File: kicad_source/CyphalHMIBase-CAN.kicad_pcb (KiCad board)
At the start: 2 copper layers, 58 x 55 mm, 62 parts, among them CN1 SM04B-SRSS-TB, CN2 DNI, CN3 SM04B-SRSS-TB, CN4 RASPBERRYPI_PICO, CN5 SM04B-GHS-TB, CN6 SM04B-GHS-TB, J1 Conn_01x08, J2 SD_Card_Device, SW1 PTS636 SM43 SMTR LFS, SW2 SW_Push, SW3 RotaryEncoder_Switch_MP, U1 M24C64-RMN6TP, U2 MCP2515T-I/SO, U3 SN65HVD230, Y1 X322516MLB4SI

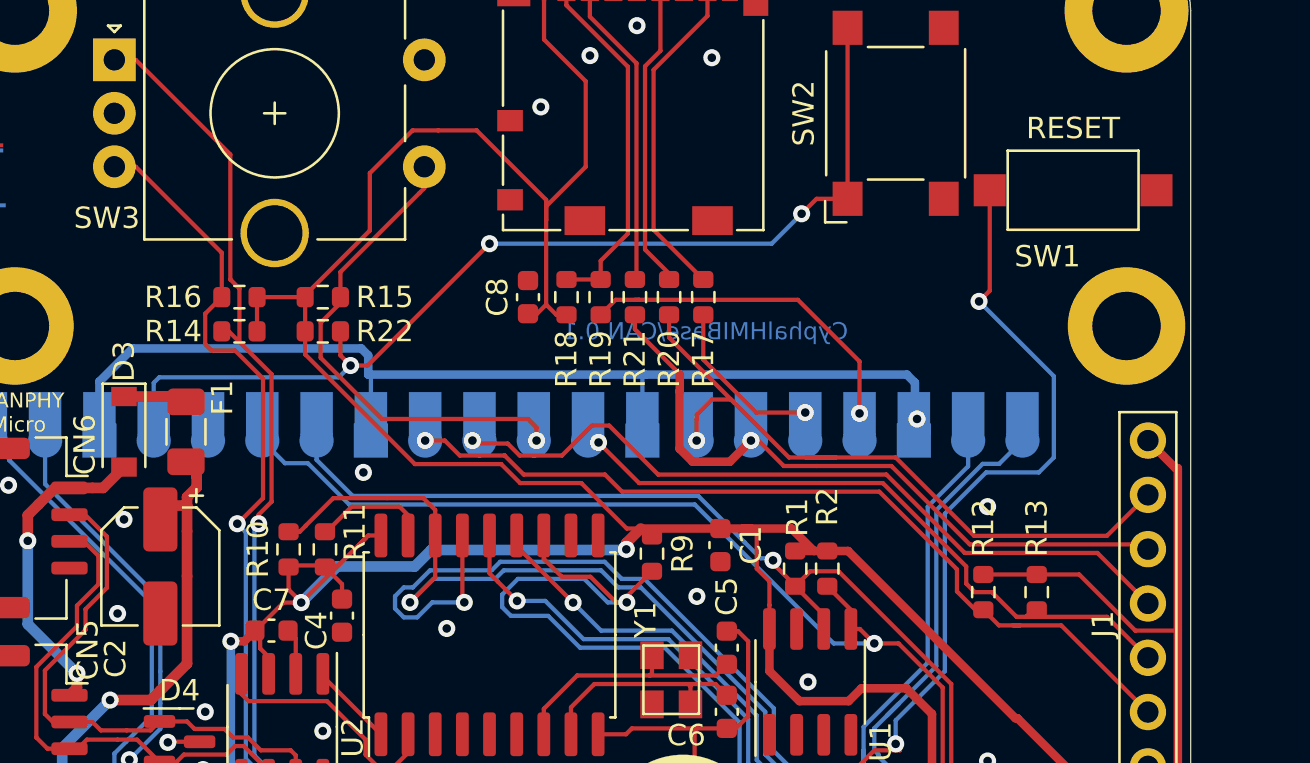
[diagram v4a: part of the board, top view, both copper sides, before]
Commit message: added backlight control
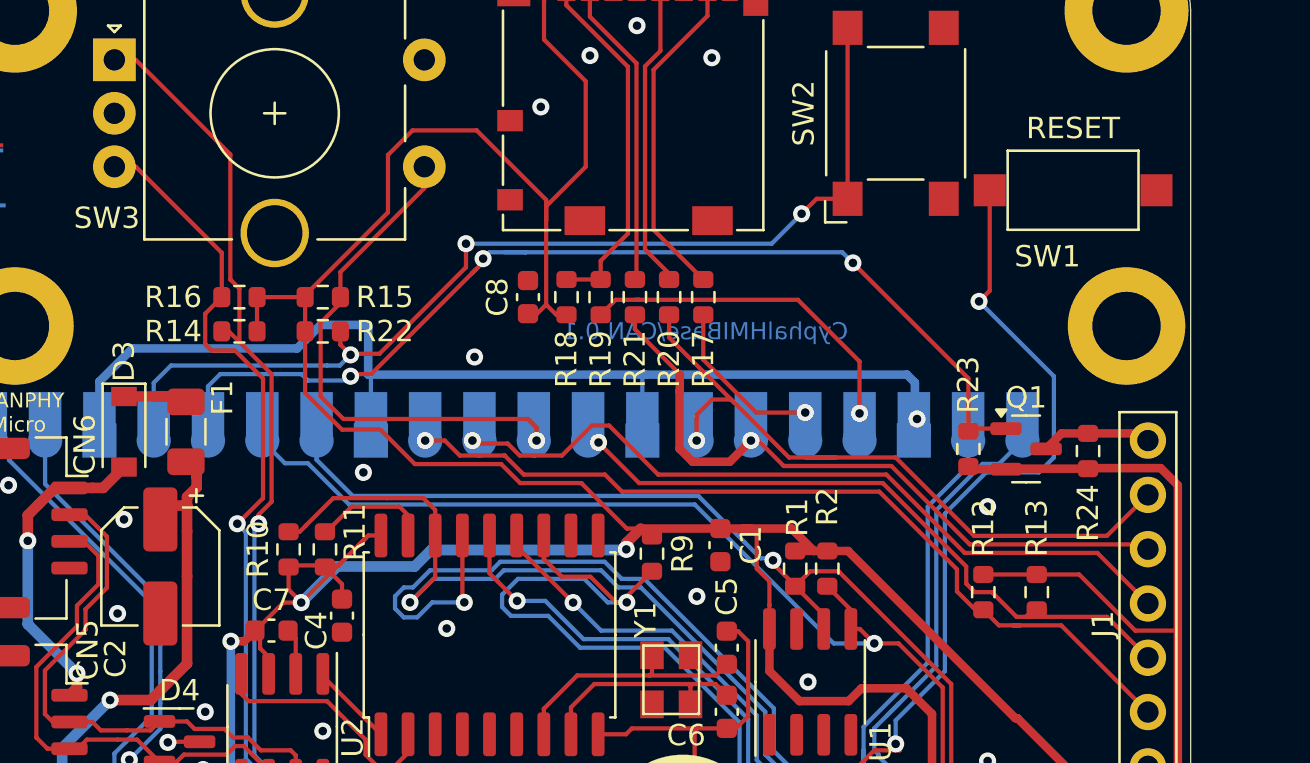
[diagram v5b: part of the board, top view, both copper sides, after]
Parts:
- added Q1: PMOS, Package_TO_SOT_SMD:SOT-23, F.Cu at (114.3, 83.5)
- added R23: 10k, Resistor_SMD:R_0603_1608Metric, F.Cu at (111.6, 83.5)
- added R24: DNI, Resistor_SMD:R_0603_1608Metric, F.Cu at (117.2, 83.6)
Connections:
- CN4 pad 5: unconnected-(CN4-GP3/SPI0_TX/I2C1_SCL-Pad5) -> TFT_BKLT
- J1 pad 8: +3V3 -> /Display/TFT_BKLT_Q
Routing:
- net TFT_BKLT: track 0.00 -> 49.3 mm, vias 0 -> 3
- net +3V3: track 216.7 -> 225.2 mm
- net /Display/TFT_BKLT_Q: track 0.00 -> 5.20 mm
- net GND: track 96.7 -> 98.4 mm, vias 23 -> 24
- net ROT_SW: track 24.3 -> 25.3 mm

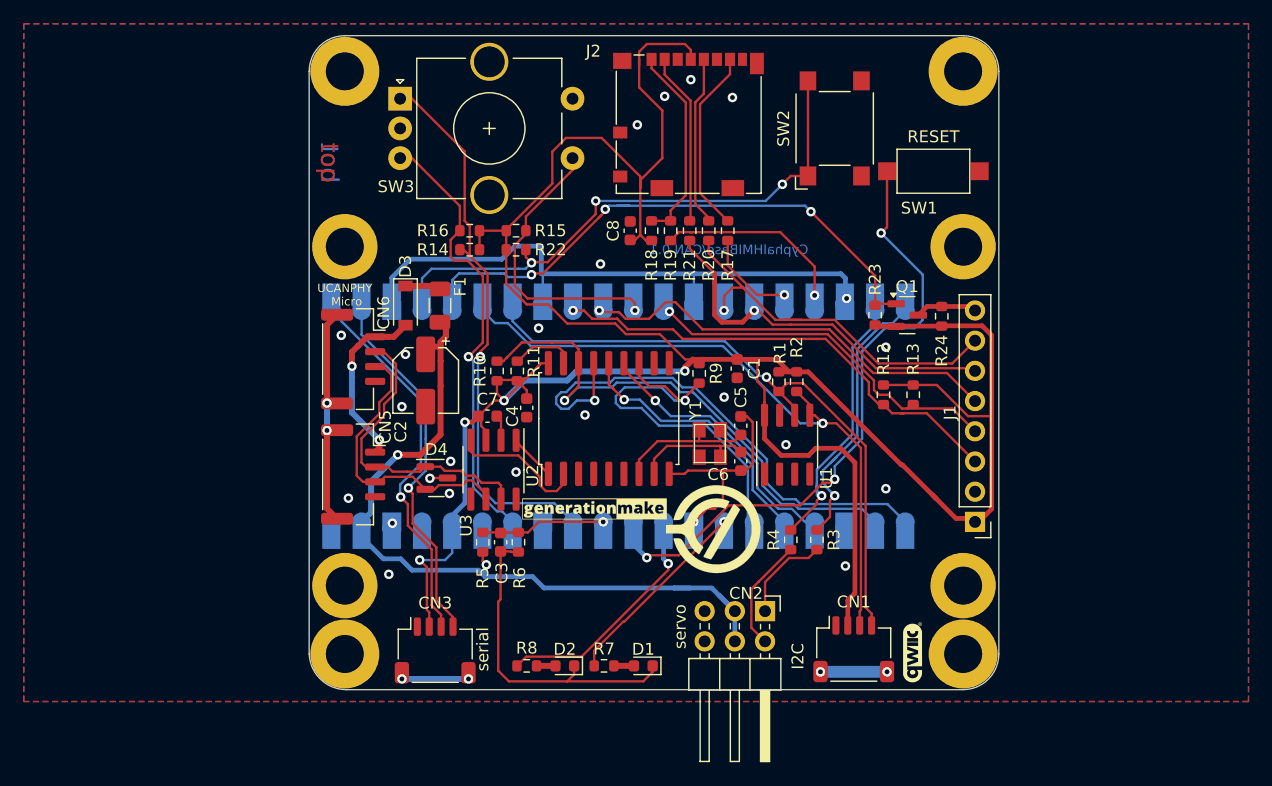
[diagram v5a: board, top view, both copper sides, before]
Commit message: fixed drc errors
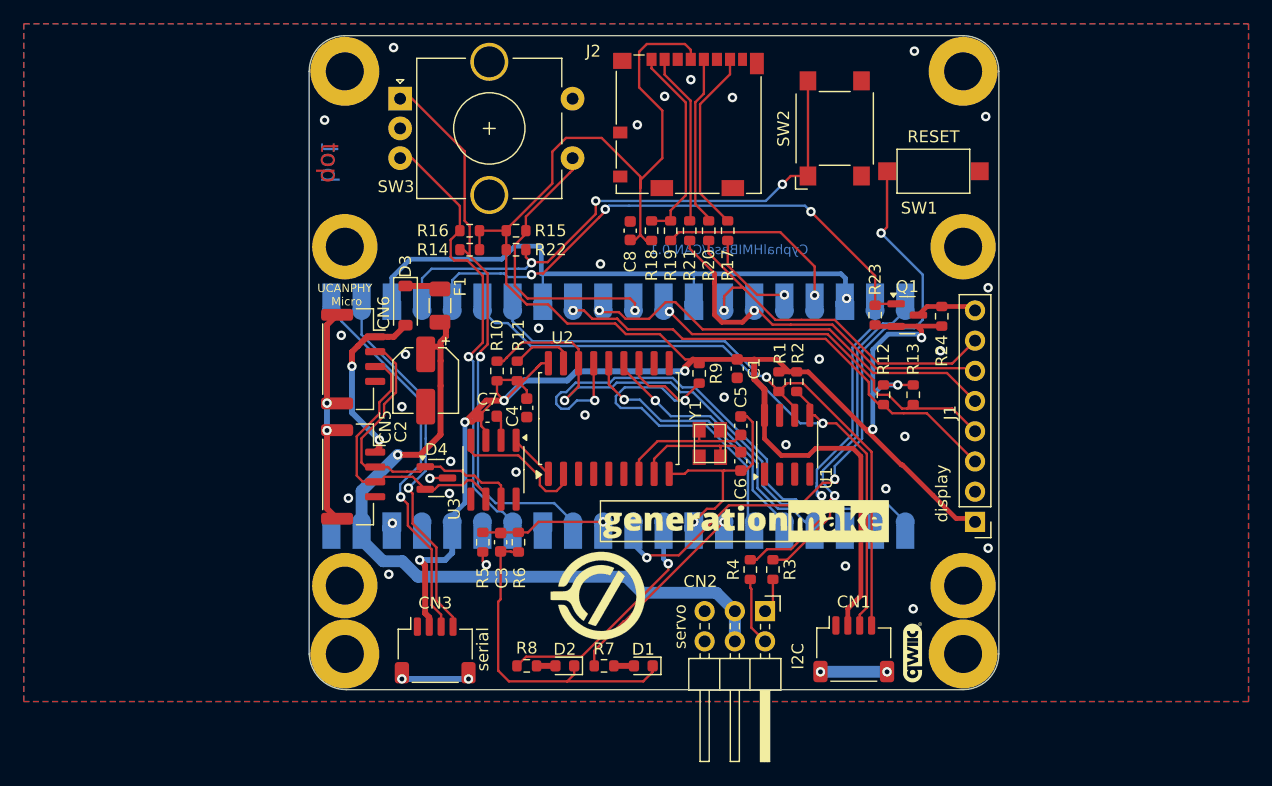
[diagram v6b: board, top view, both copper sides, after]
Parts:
- CN4: footprint generationmake:RASPI_PICO_SOLDER_Kopie -> generationmake:RASPI_PICO_SOLDER_ONLY
- L1: footprint labels:generationmake_small_silk -> generationmake:generationmake_logo
- L2: footprint labels:generationmake_small_solder -> generationmake:generationmake_small_solder
- L3: footprint labels:opencyphal_small -> generationmake:opencyphal_small
- moved L1 13.1 mm to (100.6, 106.1)
- moved L3 11.2 mm to (88.3, 107.1)
- moved L2 5.73 mm to (84.7, 113.9)
- moved R3 4.47 mm to (103.0, 104.9)
- moved R4 4.22 mm to (101.1, 104.9)
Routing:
- net +3V3: track 225.2 -> 216.5 mm, vias 4 -> 7
- net /SERVO0: track 24.5 -> 29.9 mm
- net /SERVO1_R: track 7.94 -> 2.95 mm
- net /SERVO0_R: track 9.56 -> 5.73 mm
- net (no net): track 3.81 -> 0.00 mm
- net /SERVO1: track 24.1 -> 27.6 mm
- net +BATT: track 65.9 -> 64.0 mm
- net SPI1_SCK: track 34.1 -> 32.7 mm
- net TFT_BKLT: track 49.3 -> 48.0 mm
- net GND: vias 24 -> 33
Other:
- board text added: "display"

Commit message: fixed micro sd card connector
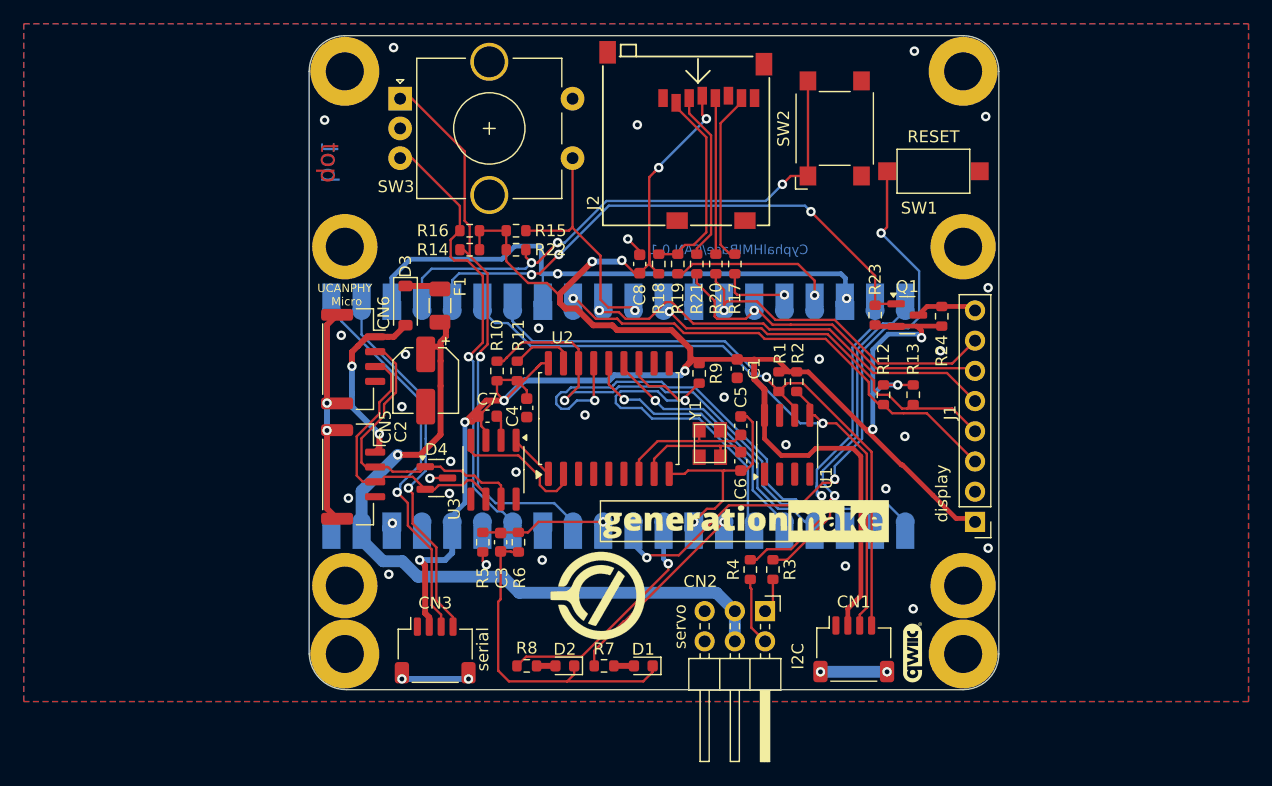
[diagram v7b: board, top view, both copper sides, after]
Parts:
- J2: value SD_Card_Device -> Micro_SD_Card; footprint Connector_Card:microSD_HC_Molex_104031-0811 -> generationmake:WE_693071010811
- moved J2 10.9 mm to (102.7, 76.0), turned to 180 degrees
- moved C8 2.91 mm to (91.8, 79.2)
- moved R18 2.86 mm to (93.4, 79.2)
- moved R20 2.86 mm to (98.2, 79.2)
- moved R17 2.86 mm to (99.8, 79.2)
- moved R19 2.86 mm to (95.0, 79.2)
- moved R21 2.86 mm to (96.6, 79.2)
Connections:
- J2 pad 1: /SD Card/SD_CS_R -> unconnected-(J2-DAT2-Pad1)
- J2 pad 2: /SD Card/SPI1_MOSI_R -> /SD Card/SD_CS_R
- J2 pad 3: GND -> /SD Card/SPI1_MOSI_R
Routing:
- net +3V3: track 216.5 -> 202.1 mm, vias 7 -> 11
- net SPI1_SCK: track 32.7 -> 28.8 mm
- net ROT_SW: track 25.3 -> 21.7 mm
- net SPI1_MOSI: track 33.1 -> 29.8 mm
- net SD_CS: track 16.0 -> 13.7 mm
- net SPI1_MISO: track 9.16 -> 7.10 mm
- net GND: track 98.4 -> 100.1 mm, vias 33 -> 32
- net /SD Card/SPI1_SCK_R: track 14.3 -> 13.1 mm
- net /SD Card/SPI1_MISO_R: track 15.6 -> 14.6 mm
- net SWITCH1: track 48.7 -> 48.1 mm
- net /RESET: track 54.5 -> 54.0 mm
